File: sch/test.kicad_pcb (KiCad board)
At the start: 2 copper layers, 54.6 x 88.9 mm, 26 parts, among them J1 Conn_01x06, J2 USB_B_Micro, J3 Conn_02x02_Counter_Clockwise, J8 Conn_02x23_Odd_Even, J9 Conn_02x23_Odd_Even, Q1 IRLML6402, U1 AP6212, U2 CP2102, U3 MCP2551-I-SN, U4 TPD2S017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

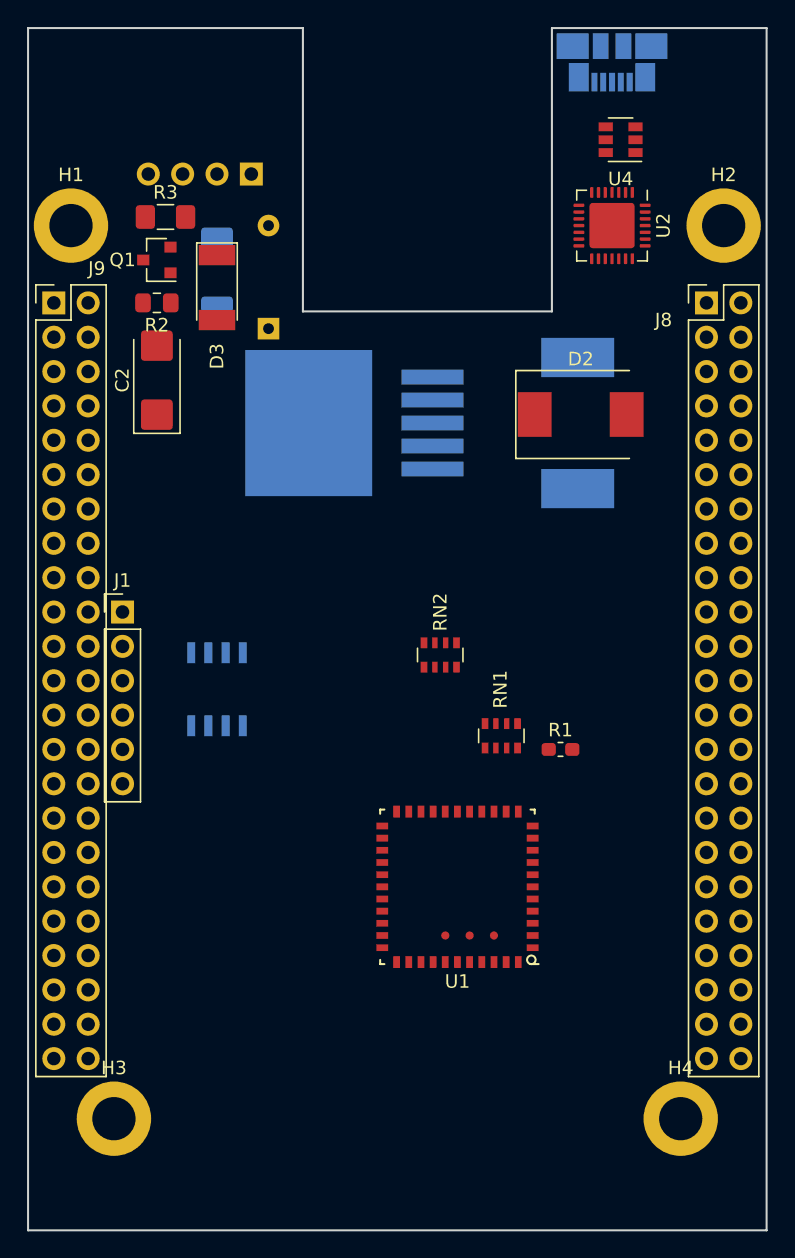
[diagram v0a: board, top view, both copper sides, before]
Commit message: add u-boot sources
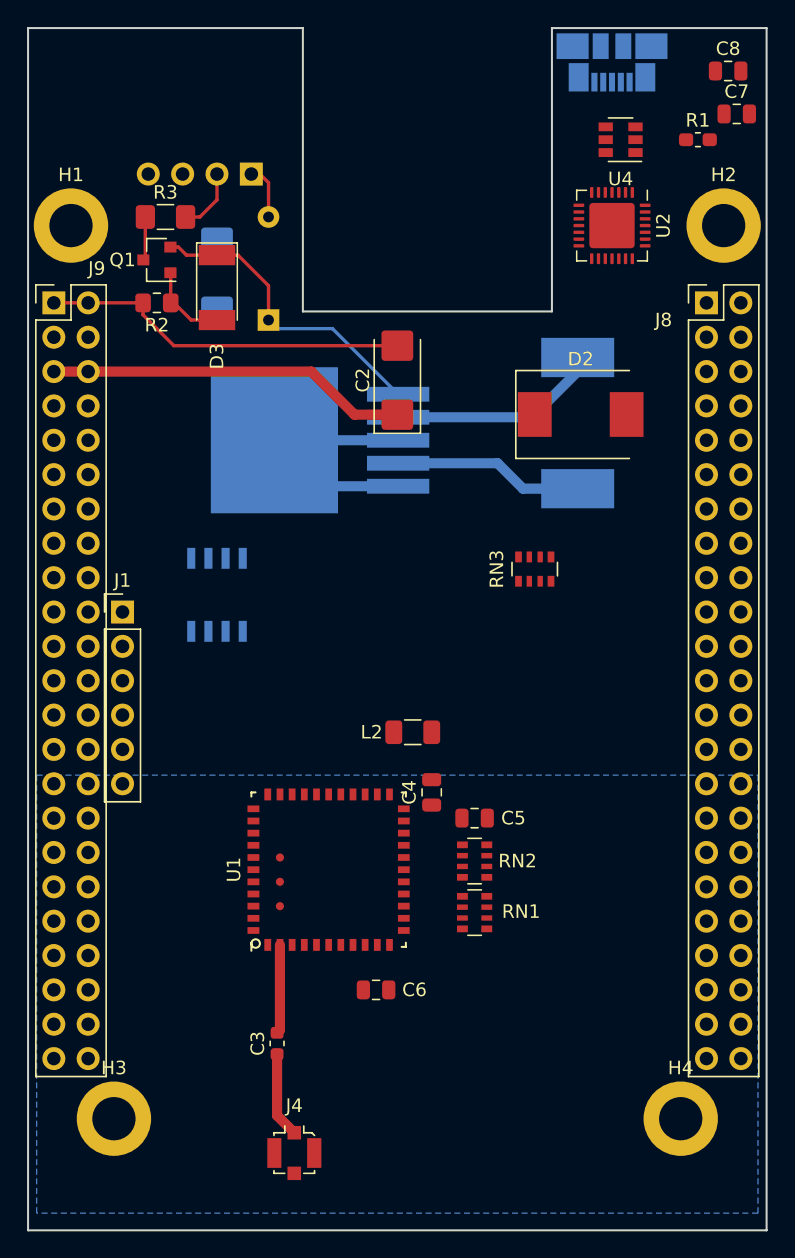
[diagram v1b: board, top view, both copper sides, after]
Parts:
- added C3: C, Capacitor_SMD:C_0603_1608Metric, F.Cu at (87.0, 104.3)
- added C4: C, Capacitor_SMD:C_0805_2012Metric, F.Cu at (98.4, 85.7)
- added C5: C, Capacitor_SMD:C_0805_2012Metric, F.Cu at (101.6, 87.6)
- added C6: C, Capacitor_SMD:C_0805_2012Metric, F.Cu at (94.3, 100.3)
- added C7: C, Capacitor_SMD:C_0805_2012Metric, F.Cu at (121.0, 35.6)
- added C8: C, Capacitor_SMD:C_0805_2012Metric, F.Cu at (120.3, 32.4)
- added J4: Conn_Coaxial, Connector_Coaxial:U.FL_Molex_MCRF_73412-0110_Vertical, F.Cu at (88.3, 112.4)
- added L2: L, Inductor_SMD:L_1206_3216Metric, F.Cu at (97.0, 81.3)
- added RN3: R_Pack04, Resistor_SMD:R_Array_Convex_4x0603, F.Cu at (106.0, 69.2)
- moved R1 46.2 mm to (118.1, 37.5)
- moved C2 17.8 mm to (95.9, 55.2)
- moved RN2 15.5 mm to (101.6, 90.8), turned to 180 degrees
- moved RN1 13.2 mm to (101.6, 94.6), turned to 180 degrees
- moved U1 9.61 mm to (90.8, 91.4), turned to 90 degrees
- moved U3 6.98 mm to (82.5, 71.1)
- moved U5 2.84 mm to (90.2, 59.7)
- moved D1 0.64 mm to (86.4, 50.8)
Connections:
- net Net-(RN1-Pad1) renamed WL_REG_ON
- net Net-(RN1-Pad2) renamed WL_HOST_WAKE
- J2 pad 1: Net-(J2-Pad1) -> Net-(C8-Pad2)
- U1 pad 22: GNDD -> +3V3
- U1 pad 9: Net-(U1-Pad9) -> +3V3
- U2 pad 25: Net-(U2-Pad25) -> B_UART0_TX
- U2 pad 26: Net-(U2-Pad26) -> B_UART0_RX
- U2 pad 7: Net-(U2-Pad7) -> Net-(C8-Pad2)
- U2 pad 8: Net-(J2-Pad1) -> Net-(C8-Pad2)
- U2 pad 9: Net-(U2-Pad9) -> Net-(R1-Pad2)
- U4 pad 5: Net-(J2-Pad1) -> Net-(C8-Pad2)
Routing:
- net GNDD: track 0.00 -> 51.0 mm
- net +5V: track 0.00 -> 41.4 mm
- net Net-(C1-Pad1): track 0.00 -> 23.2 mm
- net Net-(D2-Pad1): track 0.00 -> 16.0 mm
- net Net-(C3-Pad2): track 0.00 -> 6.59 mm
- net Net-(C3-Pad1): track 0.00 -> 6.34 mm
- net Net-(D3-Pad2): track 0.00 -> 6.18 mm
- net +12P: track 0.00 -> 4.75 mm
- net Net-(Q1-Pad3): track 0.00 -> 3.24 mm
- added copper zone on B.Cu, net GNDD
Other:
- copper layers 2 -> 4
- net class +5V added: clearance 0.4, trace_width 0.75, via_dia 0.8, via_drill 0.4
